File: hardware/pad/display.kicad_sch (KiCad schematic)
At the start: 6 parts, among them J6 OLED 1.3in SPI, U8 TPS22919DCK

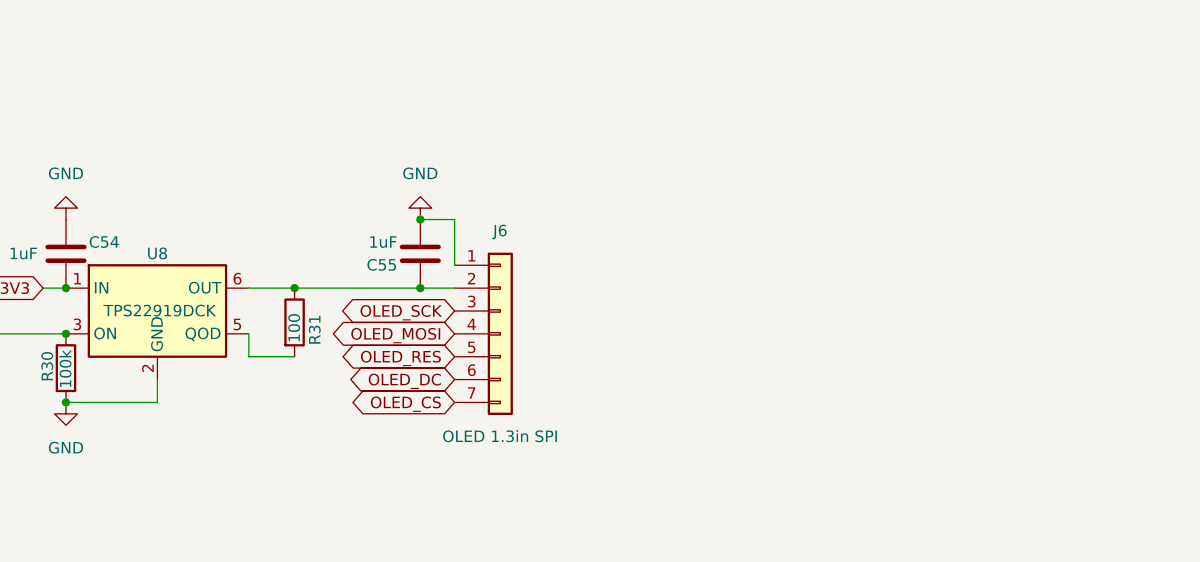
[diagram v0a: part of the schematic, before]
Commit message: Pad: display on 9-pin JST-PH with backlight MOSFET (GP27), pogo cable connector; pogo board schematic; guide updated to final refs
Co-Authored-By: Claude Opus 5.5 <noreply@anthropic.com>
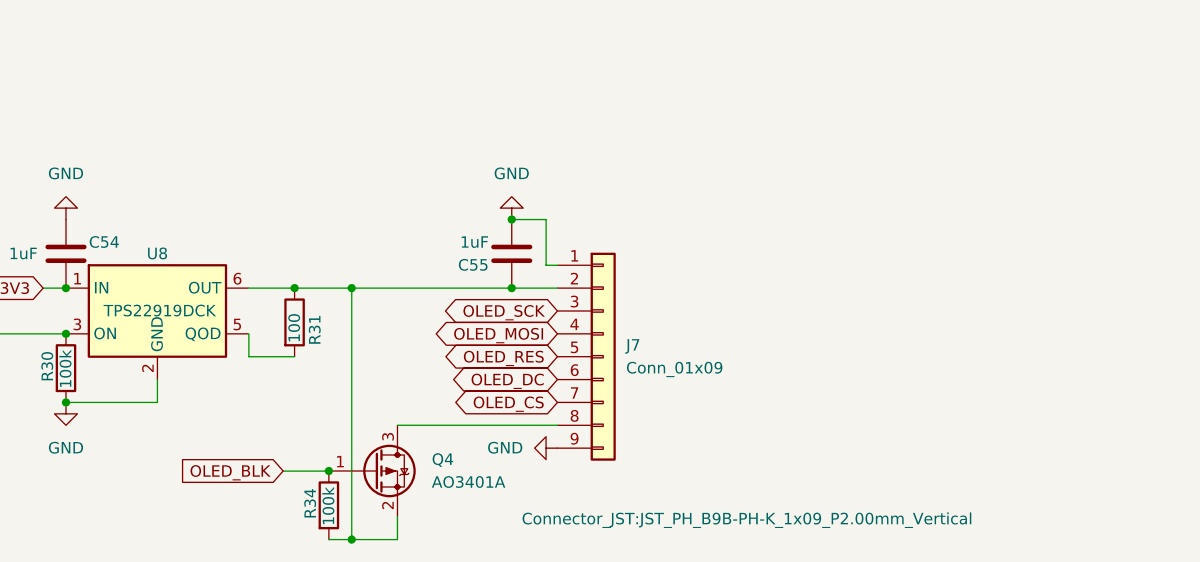
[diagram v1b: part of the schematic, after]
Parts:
- removed J6: OLED 1.3in SPI, Connector_PinSocket_2.54mm:PinSocket_1x07_P2.54mm_Vertical, symbol Connector_Generic:Conn_01x07
- added J7: Conn_01x09, Connector_JST:JST_PH_B9B-PH-K_1x09_P2.00mm_Vertical, symbol Connector_Generic:Conn_01x09
- added Q4: AO3401A, Package_TO_SOT_SMD:SOT-23, symbol Transistor_FET:AO3401A
- added R34: 100k, Resistor_SMD:R_0805_2012Metric_Pad1.20x1.40mm_HandSolder, symbol Device:R
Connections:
- net GND: now also J7.1 (Pin_1), J7.9 (Pin_9)
- net OLED_CS: now also J7.7 (Pin_7)
- net OLED_DC: now also J7.6 (Pin_6)
- net OLED_MOSI: now also J7.4 (Pin_4)
- net OLED_RES: now also J7.5 (Pin_5)
- net OLED_SCK: now also J7.3 (Pin_3)
- net at C55.1, R31.1, U8.6 (OUT): now also J7.2 (Pin_2), Q4.2 (S), R34.2
- new net: J7.8 (Pin_8), Q4.3 (D)
- new net OLED_BLK: Q4.1 (G), R34.1

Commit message: Pad PCB: first placement; SWD header removed, side-entry JST connectors, new footprints
- J4 (SWD) removed; A1 on the NoSWD Pico socket footprint (holes would sit under key 5)
- J1/J7/J2/J3 side-entry JST (S*B), J5 stays vertical
- New footprints: PEC11R encoder (13.2 mm lugs), SOIC-8-1EP hand-solder (TP4056),
  narrower SOT-563 pads
- All footprints placed on the 100 x 92 board; ring LEDs radial at R 12.7,
  encoders at 16.6 / 83.4; edge clearance rule 0.2 mm
- PCB_PLACEMENT.md and placement drawings in docs/

Co-Authored-By: Claude Opus 5.5 <noreply@anthropic.com>
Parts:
- J7: footprint Connector_JST:JST_PH_B9B-PH-K_1x09_P2.00mm_Vertical -> Connector_JST:JST_PH_S9B-PH-K_1x09_P2.00mm_Horizontal
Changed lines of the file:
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@@
 			)
 		)
-		(property "Footprint" "Connector_JST:JST_PH_B9B-PH-K_1x09_P2.00mm_Vertical"
+		(property "Footprint" "Connector_JST:JST_PH_S9B-PH-K_1x09_P2.00mm_Horizontal"
 			(at 144.272 94.234 0)
 			(show_name no)
